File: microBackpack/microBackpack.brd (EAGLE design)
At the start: 87.6 x 76.2 mm, 93 parts, among them IC1 LM324D, IC2 LM324D, J2 USB_B_PTH, J4 2X6 FEMALE, U1 ATMEGA328P_TQFP, U10 TLP185, U11 TLP185, U2 5VREG-HS, U3 CP2102N-QFN24, U4 TVS_DIODE_4PK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

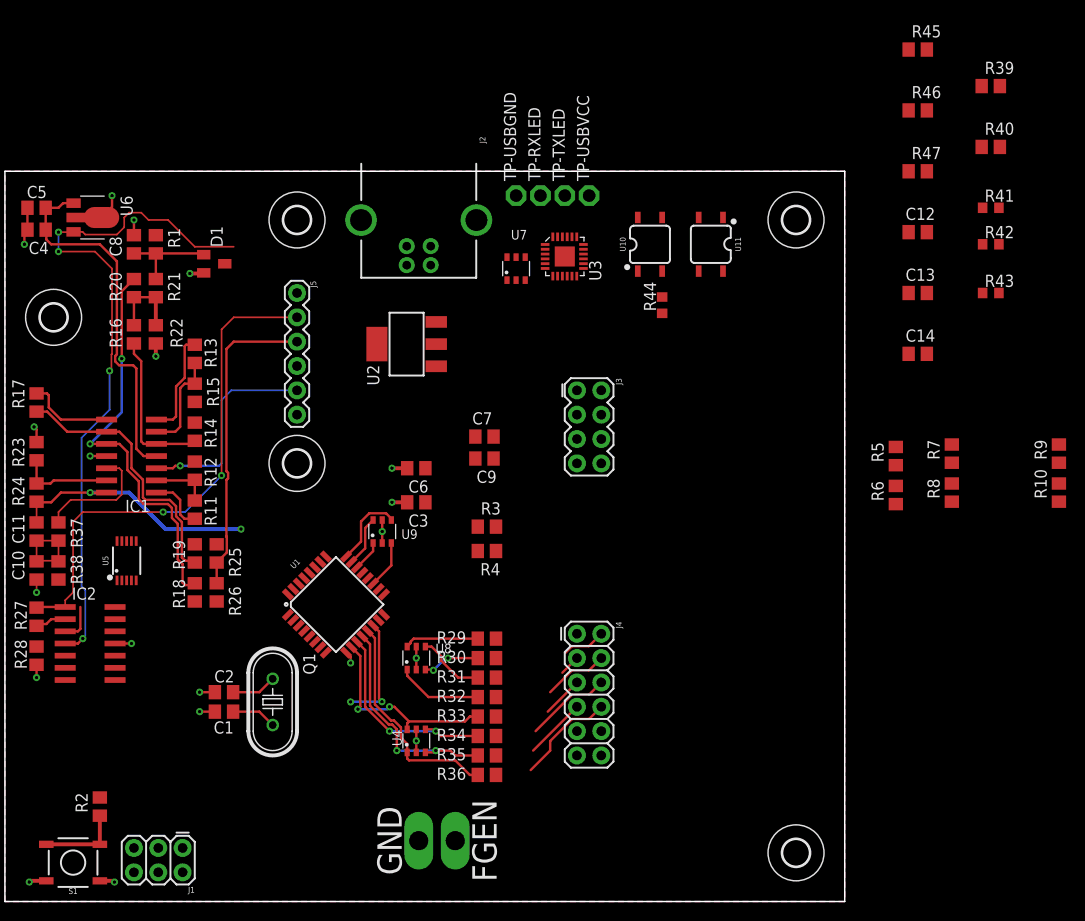
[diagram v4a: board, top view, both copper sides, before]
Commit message: Routed more traces
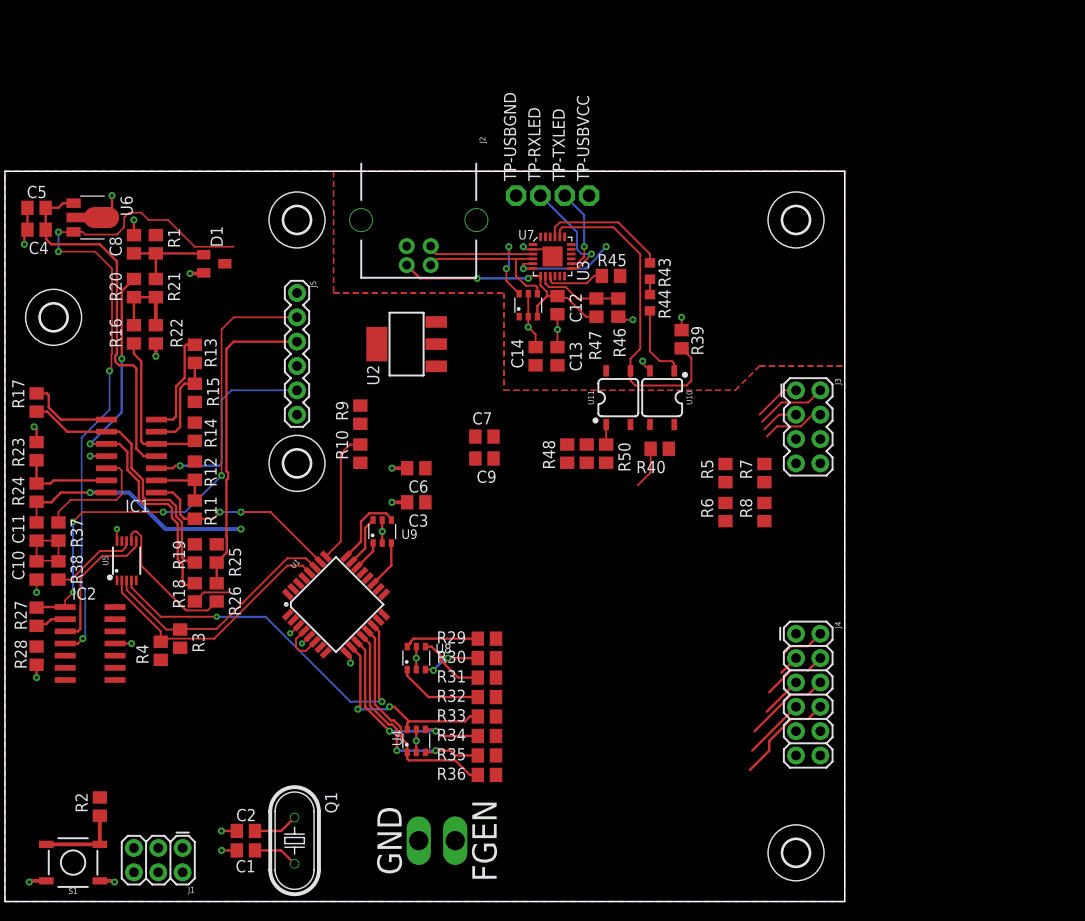
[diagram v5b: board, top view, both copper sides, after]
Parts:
- removed R41, R42: 100, rcl:R0603
- added R48, R49, R50: 1k, rcl:R0805
- moved R10 73.0 mm to (37.1, 46.7)
- moved R9 73.0 mm to (37.1, 50.8)
- moved R40 46.7 mm to (68.3, 47.2), turned to 180 degrees
- moved R39 41.7 mm to (70.6, 58.7), turned to 270 degrees
- moved C14 39.9 mm to (55.4, 56.9), turned to 90 degrees
- moved R45 39.8 mm to (63.2, 65.3)
- moved C12 38.4 mm to (57.7, 62.2), turned to 270 degrees
- moved C13 38.2 mm to (57.7, 56.9), turned to 90 degrees
- moved R46 37.4 mm to (64.0, 62.0), turned to 90 degrees
- moved R47 36.4 mm to (61.7, 62.0), turned to 270 degrees
- moved R43 35.6 mm to (67.3, 65.8), turned to 270 degrees
- moved R4 35.6 mm to (16.3, 26.2), turned to 270 degrees
- moved R3 34.1 mm to (18.3, 27.4), turned to 270 degrees
- moved J4 22.9 mm to (82.5, 27.9)
- moved J3 22.9 mm to (83.8, 49.5)
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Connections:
- removed net N$13: R41.2, R42.1
- net D+: now also U7.6; no longer U7.4
- net D-: now also U7.4; no longer U7.3
- net MCU2USB: now also R48.1, R49.1, R50.1; no longer R42.2
- net N$5: now also R48.2, R49.2, R50.2; no longer R41.1
- net VBUS: now also U7.3; no longer U7.6
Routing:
- net N$16: track 0.00 -> 34.6 mm
- net LDAC: track 11.6 -> 40.2 mm
- net SCL: track 0.00 -> 27.2 mm
- net SDA: track 0.00 -> 25.8 mm
- net VBUS: track 0.00 -> 25.6 mm, vias 0 -> 2
- net D+: track 0.00 -> 17.5 mm, vias 0 -> 2
- net USB_GND: track 0.00 -> 17.3 mm, vias 0 -> 6
- net D-: track 0.00 -> 16.1 mm
- net ADC3: track 6.03 -> 21.6 mm, vias 0 -> 2
- net DAC_B: track 0.00 -> 15.3 mm
- net ADC2: track 0.00 -> 13.8 mm
- net N$20: track 0.00 -> 13.4 mm
- net USB_VCC: track 0.00 -> 12.2 mm, vias 0 -> 2
- net N$21: track 0.00 -> 11.7 mm, vias 0 -> 1
- net DAC_A: track 3.98 -> 14.8 mm
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- added copper zone on layer 16, net USB_GND
- added copper zone on layer 1, net USB_VCC

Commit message: Moved headers and holes
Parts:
- added H6: MOUNT-HOLE2.8, holes:2,8
- moved J3 10.2 mm to (82.5, 39.4)
- moved R5 10.2 mm to (70.1, 35.8)
- moved R6 10.2 mm to (70.1, 31.8)
- moved R7 10.2 mm to (74.2, 35.8)
- moved R8 10.2 mm to (74.2, 31.8)
- moved C1 8.82 mm to (26.9, 14.0)
- moved Q1 8.82 mm to (32.0, 15.0)
- moved C2 8.82 mm to (26.9, 16.0)
- moved H4 1.27 mm to (81.3, 5.08)
- moved H5 1.27 mm to (81.3, 71.1)
- moved J4 1.27 mm to (81.3, 27.9)
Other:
- board size 87.6 x 76.2 mm -> 86.4 x 76.2 mm

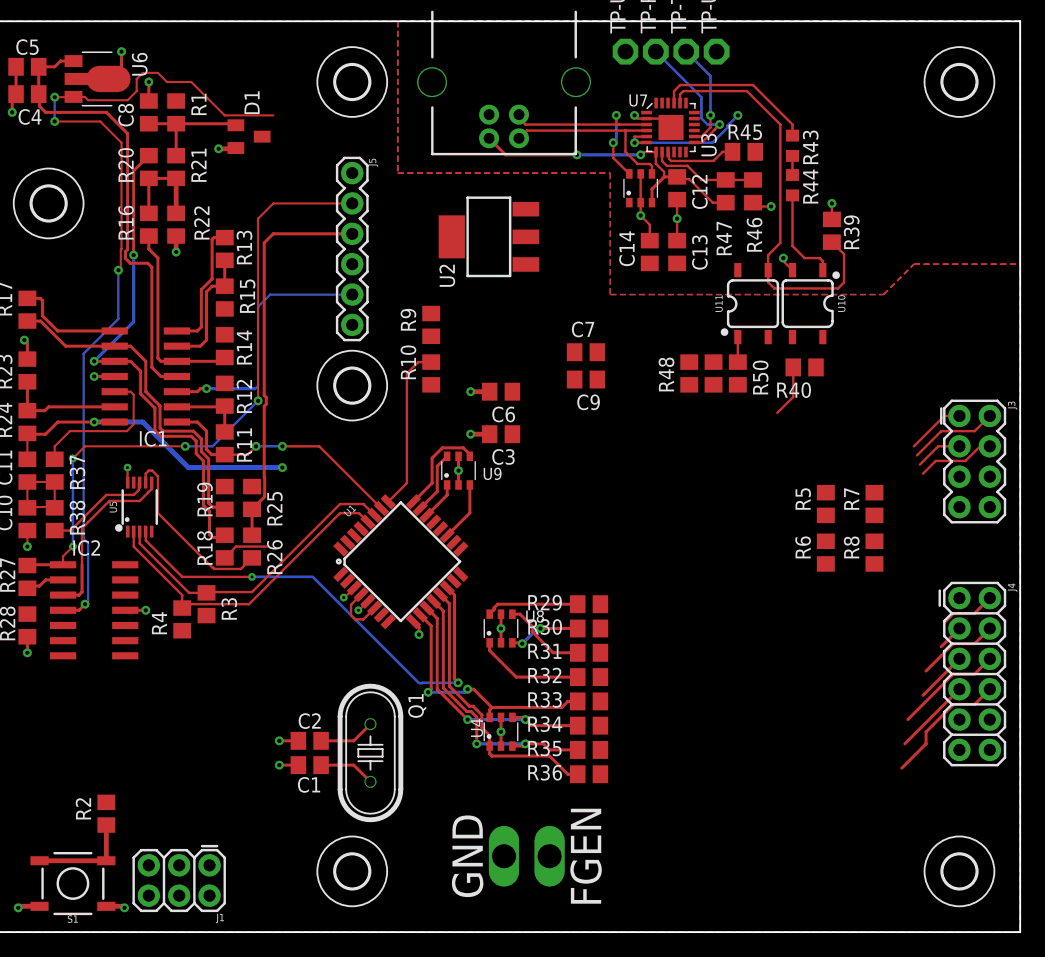
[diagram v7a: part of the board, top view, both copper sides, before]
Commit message: Routed most traces
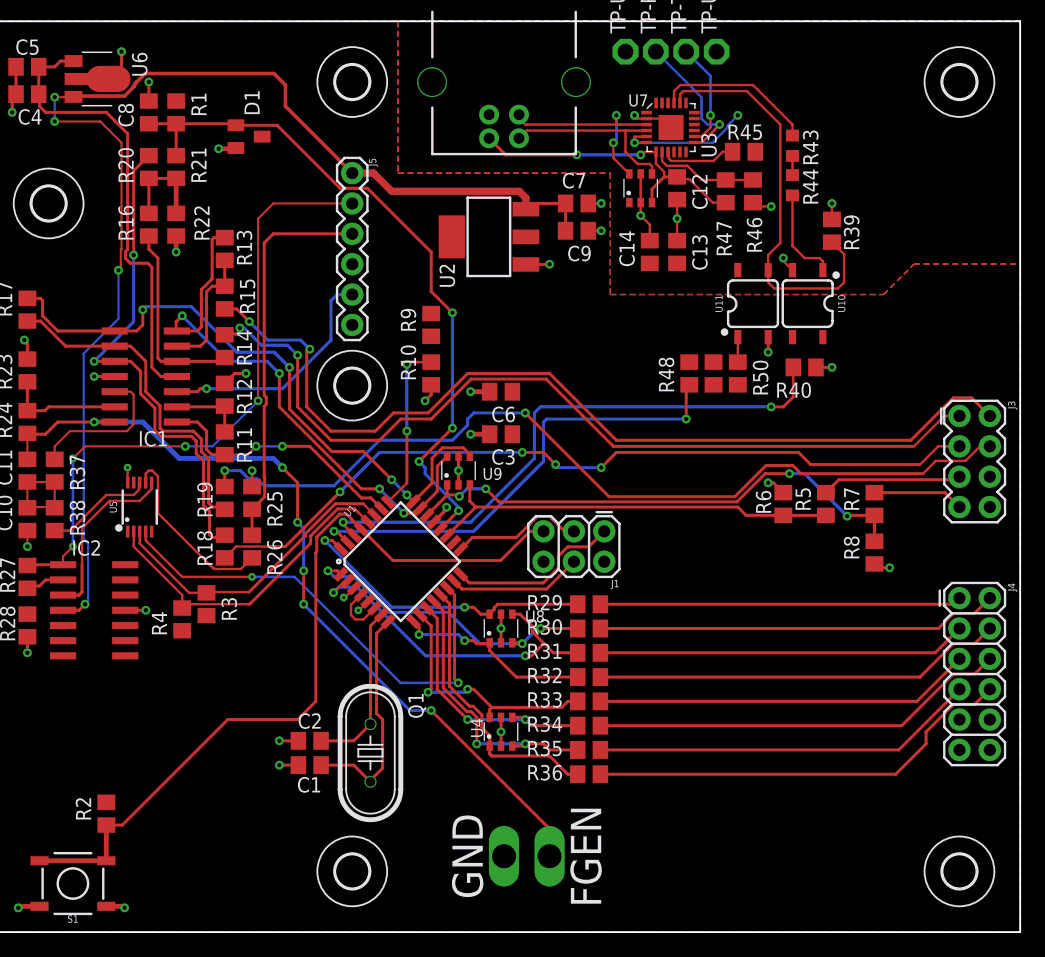
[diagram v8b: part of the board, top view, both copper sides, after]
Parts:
- moved J1 43.3 mm to (51.6, 33.5)
- moved C7 12.5 mm to (49.3, 61.0)
- moved C9 12.5 mm to (49.3, 58.7)
- moved R6 5.40 mm to (66.5, 35.8), turned to 270 degrees
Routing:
- net AD0-: track 7.46 -> 77.8 mm, vias 0 -> 2
- net AD0+: track 4.86 -> 73.8 mm, vias 0 -> 2
- net AD1-: track 6.53 -> 73.9 mm, vias 0 -> 2
- net AD1+: track 7.88 -> 67.2 mm, vias 0 -> 4
- net RESET: track 8.57 -> 66.6 mm
- net 4V_REF: track 10.0 -> 57.8 mm, vias 0 -> 4
- net USB2MCU: track 4.36 -> 48.2 mm, vias 0 -> 2
- net FGEN: track 27.2 -> 70.1 mm, vias 2 -> 6
- net ADC7: track 3.24 -> 44.4 mm, vias 0 -> 4
- net MCU2USB: track 0.00 -> 39.8 mm, vias 0 -> 2
- net ADC1: track 17.4 -> 52.8 mm, vias 0 -> 4
- net 12V: track 72.0 -> 103.0 mm
- net DIO0: track 0.00 -> 30.2 mm
- net ADC0: track 16.3 -> 46.4 mm, vias 0 -> 4
- net ADC6: track 5.02 -> 35.0 mm
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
